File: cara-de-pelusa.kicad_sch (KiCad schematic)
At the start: 23 parts, among them J1 Power bottom, J2 Stomp, J3 Power top, Q1 BC108, Q2 BC109

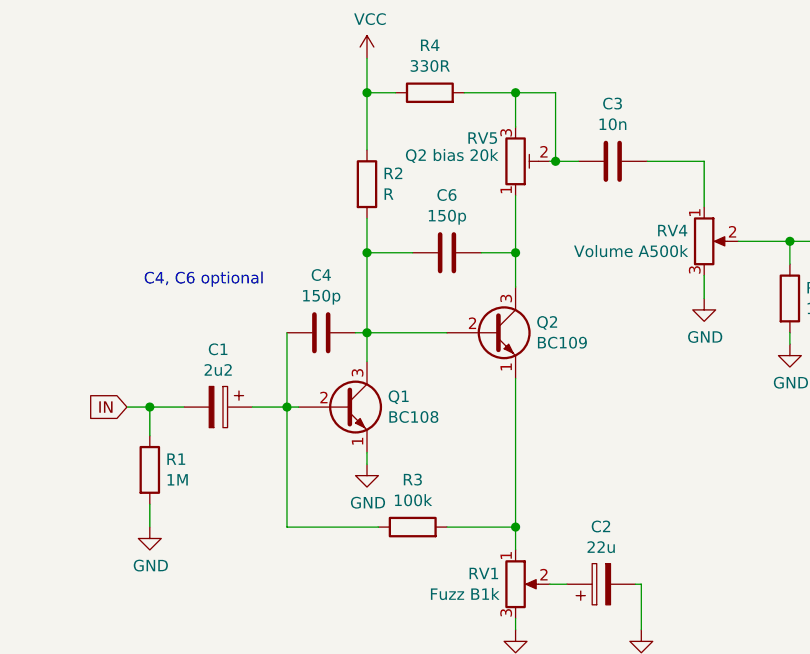
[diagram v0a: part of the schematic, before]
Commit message: 9mm onboard pots
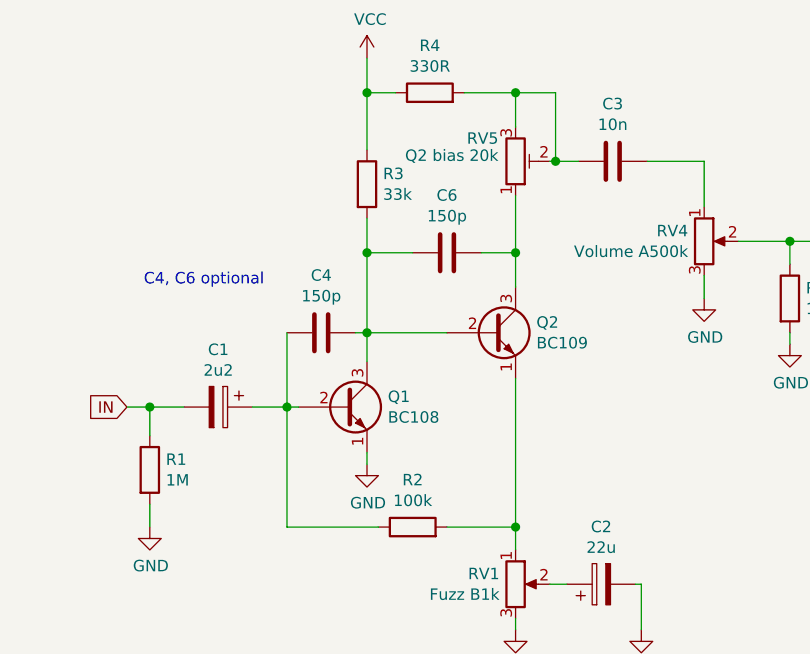
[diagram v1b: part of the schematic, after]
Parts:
- C1, C2, C5: footprint (none) -> rockola_kicad_footprints:CP_D5.0_P2.50
- C3, C4, C6, C7: footprint (none) -> rockola_kicad_footprints:C_Box_7.2_2.5
- D2: footprint (none) -> rockola_kicad_footprints:LED.3mm
- J1: footprint (none) -> rockola_kicad_footprints:Power_Header_2pin
- J2: footprint (none) -> rockola_kicad_footprints:Stomp_4pin
- J3: footprint (none) -> rockola_kicad_footprints:Power_Header_2pin_TOP
- Q1, Q2: footprint Package_TO_SOT_THT:TO-18-3 -> rockola_kicad_footprints:TO92_EBCE
- R1, R4, R5, R6: footprint (none) -> rockola_kicad_footprints:R_DIN0207
- R2: renamed from R3; footprint (none) -> rockola_kicad_footprints:R_DIN0207
- R3: renamed from R2; value R -> 33k; footprint (none) -> rockola_kicad_footprints:R_DIN0207
- RV1, RV4: footprint (none) -> rockola_kicad_footprints:9mm metal shaft
- RV5: footprint (none) -> potentiometers:TRIM1
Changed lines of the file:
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@@
       (effects (font (size 1.27 1.27)) (justify left))
     )
-    (property "Footprint" "" (id 2) (at 49.022 73.66 90)
+    (property "Footprint" "rockola_kicad_footprints:R_DIN0207" (id 2) (at 49.022 73.66 90)
       (effects (font (size 1.27 1.27)) hide)
     )
@@
   (symbol (lib_id "Device:R") (at 74.93 41.91 0) (unit 1)
     (in_bom yes) (on_board yes)
-    (property "Reference" "R2" (id 0) (at 76.7081 40.7606 0)
-      (effects (font (size 1.27 1.27)) (justify left))
-    )
-    (property "Value" "R" (id 1) (at 76.7081 43.0593 0)
-      (effects (font (size 1.27 1.27)) (justify left))
-    )
-    (property "Footprint" "" (id 2) (at 73.152 41.91 90)
+    (property "Reference" "R3" (id 0) (at 76.7081 40.7606 0)
+      (effects (font (size 1.27 1.27)) (justify left))
+    )
+    (property "Value" "33k" (id 1) (at 76.7081 43.0593 0)
+      (effects (font (size 1.27 1.27)) (justify left))
+    )
+    (property "Footprint" "rockola_kicad_footprints:R_DIN0207" (id 2) (at 73.152 41.91 90)
       (effects (font (size 1.27 1.27)) hide)
     )
@@
   (symbol (lib_id "Device:R") (at 80.01 80.01 90) (unit 1)
     (in_bom yes) (on_board yes)
-    (property "Reference" "R3" (id 0) (at 80.01 74.7838 90))
+    (property "Reference" "R2" (id 0) (at 80.01 74.7838 90))
     (property "Value" "100k" (id 1) (at 80.01 77.0825 90))
-    (property "Footprint" "" (id 2) (at 80.01 81.788 90)
+    (property "Footprint" "rockola_kicad_footprints:R_DIN0207" (id 2) (at 80.01 81.788 90)
       (effects (font (size 1.27 1.27)) hide)
     )
@@
     (property "Reference" "R4" (id 0) (at 81.915 26.5238 90))
     (property "Value" "330R" (id 1) (at 81.915 28.8225 90))
-    (property "Footprint" "" (id 2) (at 81.915 33.528 90)
+    (property "Footprint" "rockola_kicad_footprints:R_DIN0207" (id 2) (at 81.915 33.528 90)
       (effects (font (size 1.27 1.27)) hide)
     )
@@
       (effects (font (size 1.27 1.27)) (justify left))
     )
-    (property "Footprint" "" (id 2) (at 120.142 54.61 90)
+    (property "Footprint" "rockola_kicad_footprints:R_DIN0207" (id 2) (at 120.142 54.61 90)
       (effects (font (size 1.27 1.27)) hide)
     )
@@
     (property "Reference" "R6" (id 0) (at 128.27 104.6288 90))
     (property "Value" "CLR" (id 1) (at 128.27 106.9275 90))
-    (property "Footprint" "" (id 2) (at 128.27 111.633 90)
+    (property "Footprint" "rockola_kicad_footprints:R_DIN0207" (id 2) (at 128.27 111.633 90)
       (effects (font (size 1.27 1.27)) hide)
     )
@@
       (effects (font (size 1.27 1.27)) (justify left))
     )
-    (property "Footprint" "" (id 2) (at 52.705 125.73 0)
+    (property "Footprint" "rockola_kicad_footprints:Power_Header_2pin" (id 2) (at 52.705 125.73 0)
       (effects (font (size 1.27 1.27)) hide)
     )
@@
       (effects (font (size 1.27 1.27)) (justify left))
     )
-    (property "Footprint" "" (id 2) (at 53.34 111.125 0)
+    (property "Footprint" "rockola_kicad_footprints:Power_Header_2pin_TOP" (id 2) (at 53.34 111.125 0)
       (effects (font (size 1.27 1.27)) hide)
     )
@@
     (property "Reference" "D2" (id 0) (at 117.2845 104.3748 0))
     (property "Value" "LED" (id 1) (at 117.2845 106.6735 0))
-    (property "Footprint" "" (id 2) (at 117.475 109.855 0)
+    (property "Footprint" "rockola_kicad_footprints:LED.3mm" (id 2) (at 117.475 109.855 0)
       (effects (font (size 1.27 1.27)) hide)
     )
@@
     (property "Reference" "C1" (id 0) (at 58.42 60.3058 90))
     (property "Value" "2u2" (id 1) (at 58.42 62.6045 90))
-    (property "Footprint" "" (id 2) (at 54.61 67.6402 0)
+    (property "Footprint" "rockola_kicad_footprints:CP_D5.0_P2.50" (id 2) (at 54.61 67.6402 0)
       (effects (font (size 1.27 1.27)) hide)
     )
@@
     (property "Reference" "C4" (id 0) (at 69.85 52.0508 90))
     (property "Value" "150p" (id 1) (at 69.85 54.3495 90))
-    (property "Footprint" "" (id 2) (at 73.66 57.4548 0)
+    (property "Footprint" "rockola_kicad_footprints:C_Box_7.2_2.5" (id 2) (at 73.66 57.4548 0)
       (effects (font (size 1.27 1.27)) hide)
     )
@@
       (effects (font (size 1.27 1.27)) (justify left))
     )
-    (property "Footprint" "" (id 2) (at 81.6102 124.46 0)
+    (property "Footprint" "rockola_kicad_footprints:CP_D5.0_P2.50" (id 2) (at 81.6102 124.46 0)
       (effects (font (size 1.27 1.27)) hide)
     )
@@
     (property "Reference" "C6" (id 0) (at 83.82 43.1608 90))
     (property "Value" "150p" (id 1) (at 83.82 45.4595 90))
-    (property "Footprint" "" (id 2) (at 87.63 48.5648 0)
+    (property "Footprint" "rockola_kicad_footprints:C_Box_7.2_2.5" (id 2) (at 87.63 48.5648 0)
       (effects (font (size 1.27 1.27)) hide)
     )
@@
       (effects (font (size 1.27 1.27)) (justify left))
     )
-    (property "Footprint" "" (id 2) (at 93.6752 124.46 0)
+    (property "Footprint" "rockola_kicad_footprints:C_Box_7.2_2.5" (id 2) (at 93.6752 124.46 0)
       (effects (font (size 1.27 1.27)) hide)
     )
@@
     (property "Reference" "C2" (id 0) (at 100.965 79.9908 90))
     (property "Value" "22u" (id 1) (at 100.965 82.2895 90))
-    (property "Footprint" "" (id 2) (at 104.775 85.3948 0)
+    (property "Footprint" "rockola_kicad_footprints:CP_D5.0_P2.50" (id 2) (at 104.775 85.3948 0)
       (effects (font (size 1.27 1.27)) hide)
     )
@@
     (property "Reference" "C3" (id 0) (at 102.235 33.0008 90))
     (property "Value" "10n" (id 1) (at 102.235 35.2995 90))
-    (property "Footprint" "" (id 2) (at 106.045 38.4048 0)
+    (property "Footprint" "rockola_kicad_footprints:C_Box_7.2_2.5" (id 2) (at 106.045 38.4048 0)
       (effects (font (size 1.27 1.27)) hide)
     )
@@
       (effects (font (size 1.27 1.27)) (justify right))
     )
-    (property "Footprint" "" (id 2) (at 91.44 39.37 0)
+    (property "Footprint" "potentiometers:TRIM1" (id 2) (at 91.44 39.37 0)
       (effects (font (size 1.27 1.27)) hide)
     )
@@
       (effects (font (size 1.27 1.27)) (justify right))
     )
-    (property "Footprint" "" (id 2) (at 91.44 86.36 0)
+    (property "Footprint" "rockola_kicad_footprints:9mm metal shaft" (id 2) (at 91.44 86.36 0)
       (effects (font (size 1.27 1.27)) hide)
     )
@@
       (effects (font (size 1.27 1.27)) (justify right))
     )
-    (property "Footprint" "" (id 2) (at 112.395 48.26 0)
+    (property "Footprint" "rockola_kicad_footprints:9mm metal shaft" (id 2) (at 112.395 48.26 0)
       (effects (font (size 1.27 1.27)) hide)
     )
@@
       (effects (font (size 1.27 1.27)) (justify left))
     )
-    (property "Footprint" "" (id 2) (at 53.34 99.06 0)
+    (property "Footprint" "rockola_kicad_footprints:Stomp_4pin" (id 2) (at 53.34 99.06 0)
       (effects (font (size 1.27 1.27)) hide)
     )
@@
       (effects (font (size 1.27 1.27)) (justify left))
     )
-    (property "Footprint" "Package_TO_SOT_THT:TO-18-3" (id 2) (at 77.47 68.58 0)
+    (property "Footprint" "rockola_kicad_footprints:TO92_EBCE" (id 2) (at 77.47 68.58 0)
       (effects (font (size 1.27 1.27) italic) (justify left) hide)
     )
@@
       (effects (font (size 1.27 1.27)) (justify left))
     )
-    (property "Footprint" "Package_TO_SOT_THT:TO-18-3" (id 2) (at 93.98 60.325 0)
+    (property "Footprint" "rockola_kicad_footprints:TO92_EBCE" (id 2) (at 93.98 60.325 0)
       (effects (font (size 1.27 1.27) italic) (justify left) hide)
     )
@@
       (reference "R1") (unit 1)
     )
+    (path "/3af1ccb2-85cc-44da-a762-4df8b9cc1925"
+      (reference "R2") (unit 1)
+    )
     (path "/d9414375-c40f-4acd-a26c-7e295bafa3eb"
-      (reference "R2") (unit 1)
-    )
-    (path "/3af1ccb2-85cc-44da-a762-4df8b9cc1925"
       (reference "R3") (unit 1)
     )

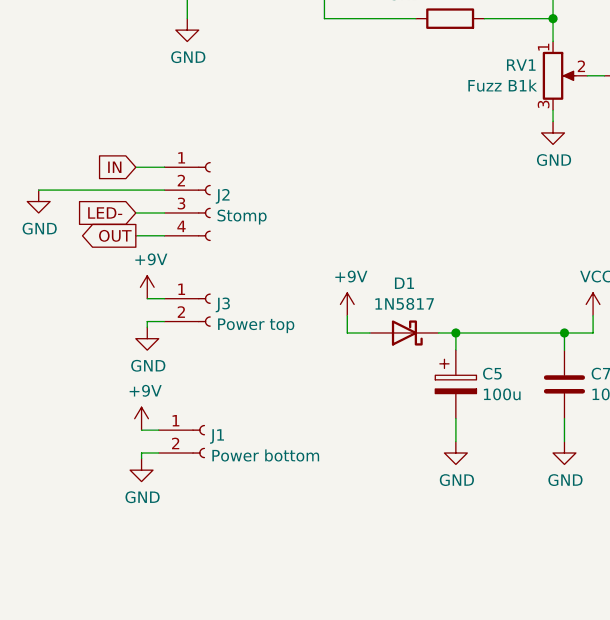
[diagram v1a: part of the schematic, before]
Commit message: updated to KiCad 6.0
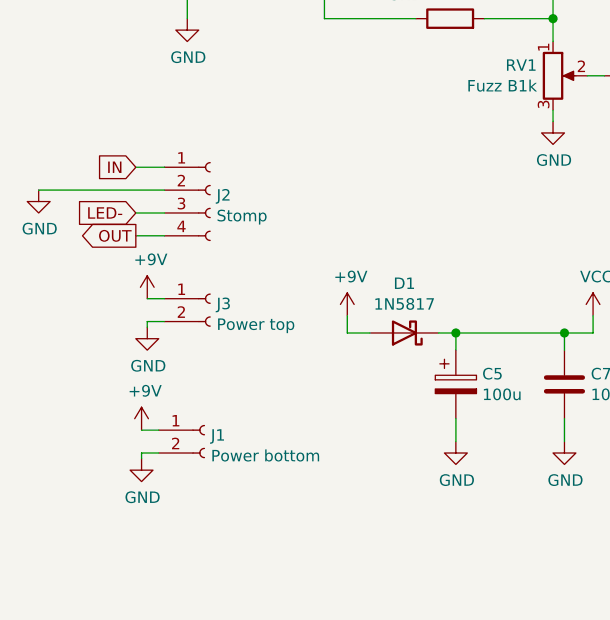
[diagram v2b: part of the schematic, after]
